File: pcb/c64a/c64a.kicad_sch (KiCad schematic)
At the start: 146 parts, among them J1 Conn_01x20_Male, SW1 1, SW10 3, SW11 W, SW12 A, SW13 L-SHIFT, SW14 Z, SW15 S, SW16 E, SW17 4, SW18 5, SW19 R, SW2 L-ARROW, SW20 D, SW21 X, SW22 C, SW23 F, SW24 T, SW25 6, SW26 7, SW27 Y, SW28 G, SW29 V, SW3 CTRL, SW30 B, SW31 H, SW32 U, SW33 8, SW34 9, SW35 I, SW36 J, SW37 N, SW38 M, SW39 K, SW4 RUN / STOP, SW40 O, SW41 0, SW42 +, SW43 P, SW44 L, SW45 ,, SW46 ., SW47 :, SW48 @, SW49 -, SW5 SPACE, SW50 POUND, SW51 *, SW52 ;, SW53 /, SW54 R-SHIFT, SW55 =, SW56 UP-ARROW, SW57 HOME, SW58 RESTORE, SW59 DEL, SW6 COMMODORE, SW60 RETURN, SW61 LEFT-RIGHT, SW62 UP-DOWN, SW63 F1, SW64 F3, SW65 F5, SW66 F7, SW7 Q, SW8 2, SW9 SHIFT-LOCK

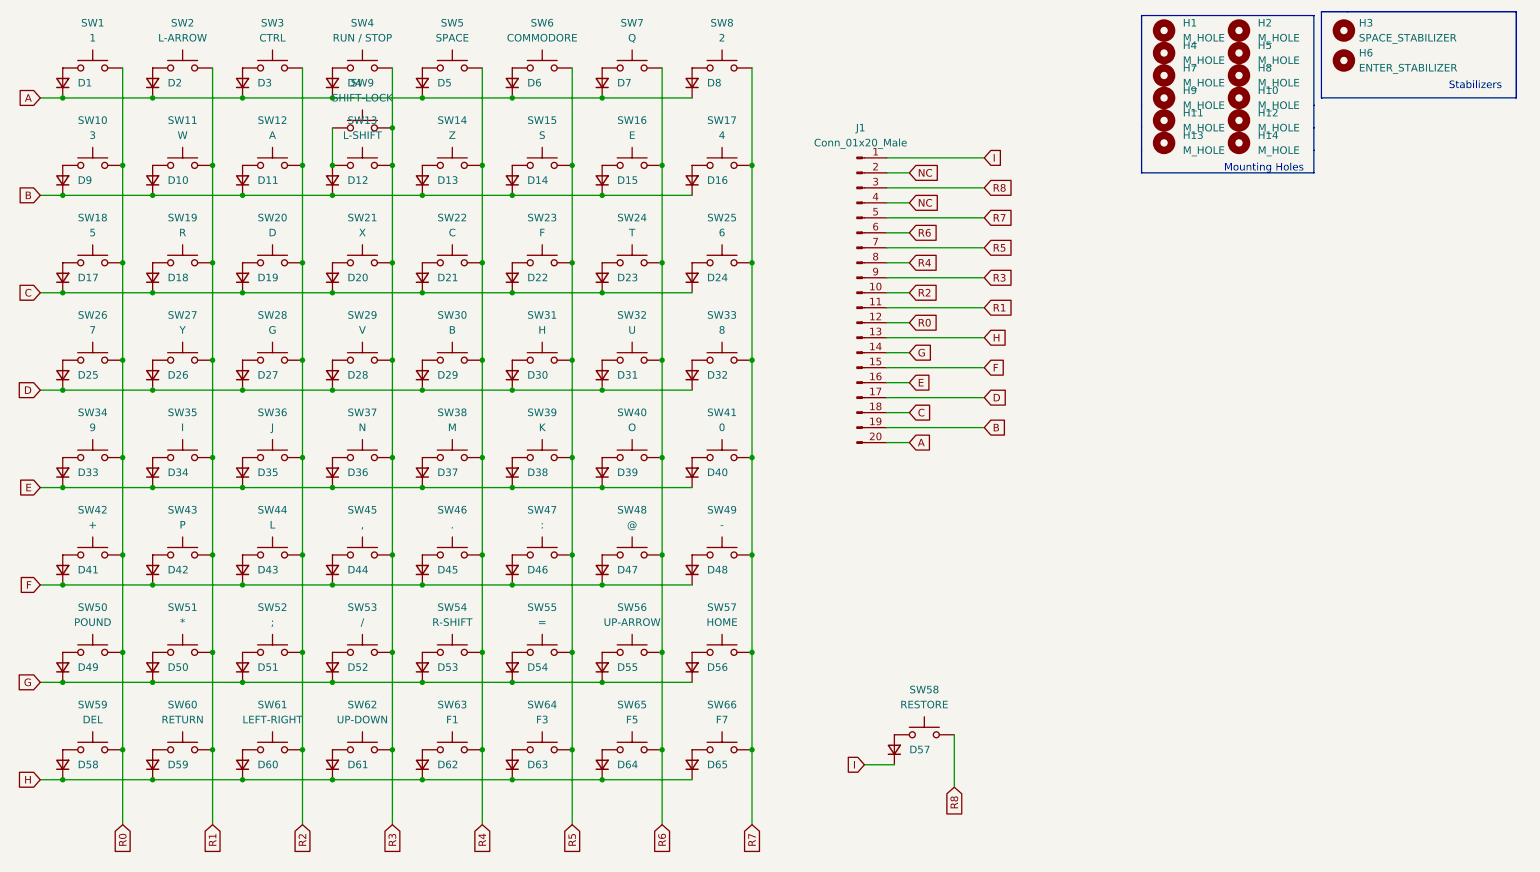
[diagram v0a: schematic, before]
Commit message: Switches changed to 5 pin
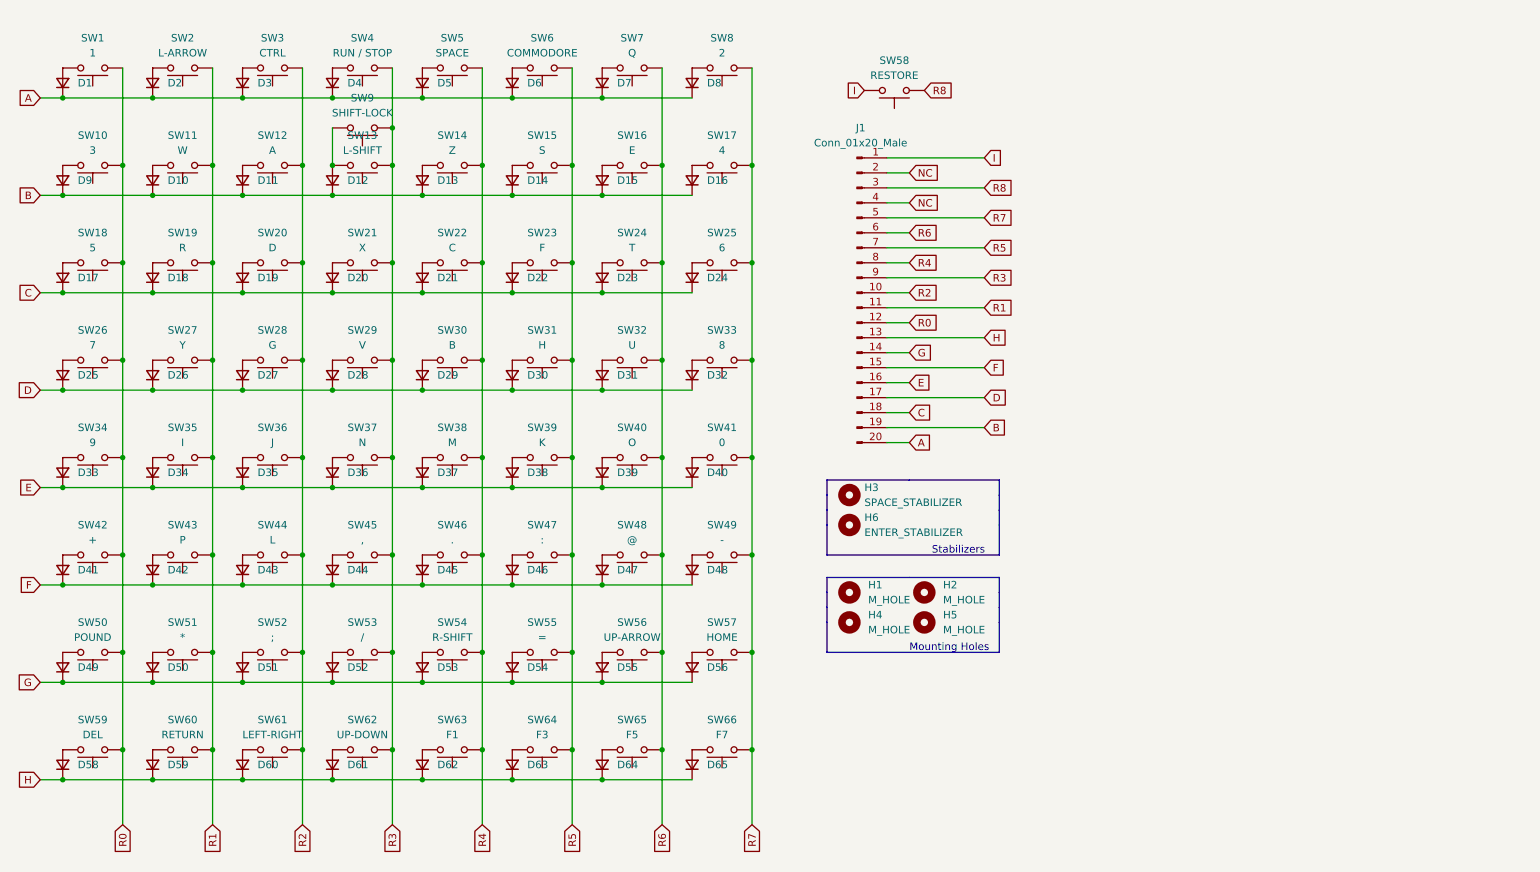
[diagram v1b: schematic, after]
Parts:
- removed D57: D_Small, Diode_SMD:D_SOD-123, symbol Device:D_Small
- removed H10, H11, H12, H13, H14, H7, H8, H9: M_HOLE, MountingHole:MountingHole_2.2mm_M2, symbol Mechanical:MountingHole
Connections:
- net I: now also SW58.2
- net R0: now also SW1.1, SW10.1, SW18.1, SW26.1, SW34.1, SW42.1, SW50.1, SW59.1; no longer SW1.2, SW10.2, SW18.2, SW26.2, SW34.2, SW42.2, SW50.2, SW59.2
- net R1: now also SW11.1, SW19.1, SW2.1, SW27.1, SW35.1, SW43.1, SW51.1, SW60.1; no longer SW11.2, SW19.2, SW2.2, SW27.2, SW35.2, SW43.2, SW51.2, SW60.2
- net R2: now also SW12.1, SW20.1, SW28.1, SW3.1, SW36.1, SW44.1, SW52.1, SW61.1; no longer SW12.2, SW20.2, SW28.2, SW3.2, SW36.2, SW44.2, SW52.2, SW61.2
- net R3: now also SW13.1, SW21.1, SW29.1, SW37.1, SW4.1, SW45.1, SW53.1, SW62.1, SW9.1; no longer SW13.2, SW21.2, SW29.2, SW37.2, SW4.2, SW45.2, SW53.2, SW62.2, SW9.2
- net R4: now also SW14.1, SW22.1, SW30.1, SW38.1, SW46.1, SW5.1, SW54.1, SW63.1; no longer SW14.2, SW22.2, SW30.2, SW38.2, SW46.2, SW5.2, SW54.2, SW63.2
- net R5: now also SW15.1, SW23.1, SW31.1, SW39.1, SW47.1, SW55.1, SW6.1, SW64.1; no longer SW15.2, SW23.2, SW31.2, SW39.2, SW47.2, SW55.2, SW6.2, SW64.2
- net R6: now also SW16.1, SW24.1, SW32.1, SW40.1, SW48.1, SW56.1, SW65.1, SW7.1; no longer SW16.2, SW24.2, SW32.2, SW40.2, SW48.2, SW56.2, SW65.2, SW7.2
- net R7: now also SW17.1, SW25.1, SW33.1, SW41.1, SW49.1, SW57.1, SW66.1, SW8.1; no longer SW17.2, SW25.2, SW33.2, SW41.2, SW49.2, SW57.2, SW66.2, SW8.2
- net R8: now also SW58.1; no longer SW58.2
- net at D11.2 (A): now also SW12.2; no longer SW12.1
- net at D63.2 (A): now also SW64.2; no longer SW64.1
- net at D22.2 (A): now also SW23.2; no longer SW23.1
- net at D48.2 (A): now also SW49.2; no longer SW49.1
- net at D15.2 (A): now also SW16.2; no longer SW16.1
- net at D9.2 (A): now also SW10.2; no longer SW10.1
- net at D4.2 (A): now also SW4.2; no longer SW4.1
- net at D6.2 (A): now also SW6.2; no longer SW6.1
- net at D37.2 (A): now also SW38.2; no longer SW38.1
- net at D54.2 (A): now also SW55.2; no longer SW55.1
- net at D39.2 (A): now also SW40.2; no longer SW40.1
- net at D35.2 (A): now also SW36.2; no longer SW36.1
- net at D26.2 (A): now also SW27.2; no longer SW27.1
- net at D47.2 (A): now also SW48.2; no longer SW48.1
- net at D8.2 (A): now also SW8.2; no longer SW8.1
- net at D59.2 (A): now also SW60.2; no longer SW60.1
- net at D41.2 (A): now also SW42.2; no longer SW42.1
- net at D17.2 (A): now also SW18.2; no longer SW18.1
- net at D10.2 (A): now also SW11.2; no longer SW11.1
- net at D53.2 (A): now also SW54.2; no longer SW54.1
- net at D20.2 (A): now also SW21.2; no longer SW21.1
- net at D40.2 (A): now also SW41.2; no longer SW41.1
- net at D34.2 (A): now also SW35.2; no longer SW35.1
- net at D65.2 (A): now also SW66.2; no longer SW66.1
- net at D55.2 (A): now also SW56.2; no longer SW56.1
- net at D27.2 (A): now also SW28.2; no longer SW28.1
- net at D46.2 (A): now also SW47.2; no longer SW47.1
- net at D58.2 (A): now also SW59.2; no longer SW59.1
- net at D38.2 (A): now also SW39.2; no longer SW39.1
- net at D62.2 (A): now also SW63.2; no longer SW63.1
- net at D3.2 (A): now also SW3.2; no longer SW3.1
- net at D30.2 (A): now also SW31.2; no longer SW31.1
- net at D44.2 (A): now also SW45.2; no longer SW45.1
- net at D25.2 (A): now also SW26.2; no longer SW26.1
- net at D43.2 (A): now also SW44.2; no longer SW44.1
- net at D19.2 (A): now also SW20.2; no longer SW20.1
- net at D29.2 (A): now also SW30.2; no longer SW30.1
- net at D31.2 (A): now also SW32.2; no longer SW32.1
- net at D28.2 (A): now also SW29.2; no longer SW29.1
- net at D51.2 (A): now also SW52.2; no longer SW52.1
- net at D21.2 (A): now also SW22.2; no longer SW22.1
- net at D45.2 (A): now also SW46.2; no longer SW46.1
- net at D1.2 (A): now also SW1.2; no longer SW1.1
- net at D5.2 (A): now also SW5.2; no longer SW5.1
- net at D52.2 (A): now also SW53.2; no longer SW53.1
- net at D36.2 (A): now also SW37.2; no longer SW37.1
- net at D7.2 (A): now also SW7.2; no longer SW7.1
- net at D2.2 (A): now also SW2.2; no longer SW2.1
- net at D64.2 (A): now also SW65.2; no longer SW65.1
- net at D16.2 (A): now also SW17.2; no longer SW17.1
- net at D60.2 (A): now also SW61.2; no longer SW61.1
- net at D56.2 (A): now also SW57.2; no longer SW57.1
- net at D61.2 (A): now also SW62.2; no longer SW62.1
- net at D24.2 (A): now also SW25.2; no longer SW25.1
- net at D13.2 (A): now also SW14.2; no longer SW14.1
- net at D49.2 (A): now also SW50.2; no longer SW50.1
- net at D14.2 (A): now also SW15.2; no longer SW15.1
- net at D18.2 (A): now also SW19.2; no longer SW19.1
- net at D23.2 (A): now also SW24.2; no longer SW24.1
- net at D33.2 (A): now also SW34.2; no longer SW34.1
- net at D42.2 (A): now also SW43.2; no longer SW43.1
- net at D32.2 (A): now also SW33.2; no longer SW33.1
- net at D50.2 (A): now also SW51.2; no longer SW51.1
- new net: D12.2 (A), SW13.2, SW9.2
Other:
- moved on the sheet: H1, H2, H3, H4, H5, H6, SW1, SW10, SW11, SW12, SW13, SW14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

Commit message: Mount cover + pcb fixes
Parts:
- J1: footprint Connector_PinHeader_1.00mm:PinHeader_1x20_P1.00mm_Horizontal -> Connector_PinHeader_1.27mm:PinHeader_1x20_P1.27mm_Horizontal
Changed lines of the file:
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@@
     (property "Reference" "J1" (id 0) (at 170.815 35.56 0))
     (property "Value" "Conn_01x20_Male" (id 1) (at 170.815 38.1 0))
-    (property "Footprint" "Connector_PinHeader_1.00mm:PinHeader_1x20_P1.00mm_Horizontal" (id 2) (at 170.18 63.5 0)
+    (property "Footprint" "Connector_PinHeader_1.27mm:PinHeader_1x20_P1.27mm_Horizontal" (id 2) (at 170.18 63.5 0)
       (effects (font (size 1.27 1.27)) hide)
     )
@@
     )
     (path "/50d77f76-2263-4e5b-952f-03c8b908276f"
-      (reference "J1") (unit 1) (value "Conn_01x20_Male") (footprint "Connector_PinHeader_1.00mm:PinHeader_1x20_P1.00mm_Horizontal")
+      (reference "J1") (unit 1) (value "Conn_01x20_Male") (footprint "Connector_PinHeader_1.27mm:PinHeader_1x20_P1.27mm_Horizontal")
     )
     (path "/6b258f22-926d-4192-b794-d0d003b1d1f3"

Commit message: Fixing spacing issues
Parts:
- removed H1, H2, H4, H5: M_HOLE, MountingHole:MountingHole_2.2mm_M2, symbol Mechanical:MountingHole
- J1: footprint Connector_PinHeader_1.27mm:PinHeader_1x20_P1.27mm_Horizontal -> Connector_PinHeader_2.54mm:PinHeader_1x20_P2.54mm_Horizontal
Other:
- note removed: "Mounting Holes"
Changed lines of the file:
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@@
   (junction (at 45.72 58.42) (diameter 0) (color 0 0 0 0)
   )
-  (polyline (pts (xy 194.31 124.46) (xy 165.1 124.46))
-    (stroke (width 0) (type default) (color 0 0 0 0))
-  )
   (wire (pts (xy 31.75 63.5) (xy 35.56 63.5))
     (stroke (width 0) (type default) (color 0 0 0 0))
@@
     (stroke (width 0) (type default) (color 0 0 0 0))
   )
-  (polyline (pts (xy 165.1 111.76) (xy 179.07 111.76))
-    (stroke (width 0) (type default) (color 0 0 0 0))
-  )
   (wire (pts (xy 96.52 46.99) (xy 111.76 46.99))
     (stroke (width 0) (type default) (color 0 0 0 0))
@@
     (stroke (width 0) (type default) (color 0 0 0 0))
   )
-  (polyline (pts (xy 165.1 124.46) (xy 165.1 119.38))
-    (stroke (width 0) (type default) (color 0 0 0 0))
-  )
   (wire (pts (xy 96.52 129.54) (xy 111.76 129.54))
     (stroke (width 0) (type default) (color 0 0 0 0))
@@
     (stroke (width 0) (type default) (color 0 0 0 0))
   )
-  (polyline (pts (xy 194.31 111.76) (xy 194.31 114.3))
-    (stroke (width 0) (type default) (color 0 0 0 0))
-  )
   (wire (pts (xy 111.76 96.52) (xy 127 96.52))
     (stroke (width 0) (type default) (color 0 0 0 0))
@@
     (stroke (width 0) (type default) (color 0 0 0 0))
   )
-  (polyline (pts (xy 194.31 114.3) (xy 194.31 116.84))
-    (stroke (width 0) (type default) (color 0 0 0 0))
-  )
   (wire (pts (xy 152.4 74.93) (xy 152.4 91.44))
     (stroke (width 0) (type default) (color 0 0 0 0))
   )
-  (polyline (pts (xy 165.1 119.38) (xy 165.1 116.84))
-    (stroke (width 0) (type default) (color 0 0 0 0))
-  )
   (wire (pts (xy 31.75 96.52) (xy 35.56 96.52))
     (stroke (width 0) (type default) (color 0 0 0 0))
@@
     (stroke (width 0) (type default) (color 0 0 0 0))
   )
-  (polyline (pts (xy 165.1 116.84) (xy 165.1 114.3))
-    (stroke (width 0) (type default) (color 0 0 0 0))
-  )
   (wire (pts (xy 179.07 63.5) (xy 175.26 63.5))
     (stroke (width 0) (type default) (color 0 0 0 0))
@@
     (stroke (width 0) (type default) (color 0 0 0 0))
   )
-  (polyline (pts (xy 165.1 114.3) (xy 165.1 111.76))
-    (stroke (width 0) (type default) (color 0 0 0 0))
-  )
   (polyline (pts (xy 179.07 95.25) (xy 194.31 95.25))
     (stroke (width 0) (type default) (color 0 0 0 0))
@@
     (stroke (width 0) (type default) (color 0 0 0 0))
   )
-  (polyline (pts (xy 194.31 116.84) (xy 194.31 119.38))
-    (stroke (width 0) (type default) (color 0 0 0 0))
-  )
   (wire (pts (xy 45.72 58.42) (xy 45.72 74.93))
     (stroke (width 0) (type default) (color 0 0 0 0))
@@
     (stroke (width 0) (type default) (color 0 0 0 0))
   )
-  (polyline (pts (xy 179.07 111.76) (xy 194.31 111.76))
-    (stroke (width 0) (type default) (color 0 0 0 0))
-  )
   (wire (pts (xy 81.28 146.05) (xy 96.52 146.05))
     (stroke (width 0) (type default) (color 0 0 0 0))
@@
     (stroke (width 0) (type default) (color 0 0 0 0))
   )
-  (polyline (pts (xy 194.31 119.38) (xy 194.31 124.46))
-    (stroke (width 0) (type default) (color 0 0 0 0))
-  )
   (wire (pts (xy 76.2 74.93) (xy 76.2 91.44))
     (stroke (width 0) (type default) (color 0 0 0 0))
@@
   (wire (pts (xy 179.07 73.66) (xy 175.26 73.66))
     (stroke (width 0) (type default) (color 0 0 0 0))
-  )
-  (text "Mounting Holes" (at 179.07 124.46 0)
-    (effects (font (size 1.27 1.27)) (justify left bottom))
   )
   (text "Stabilizers" (at 182.88 107.95 0)
@@
     (property "Reference" "J1" (id 0) (at 170.815 35.56 0))
     (property "Value" "Conn_01x20_Male" (id 1) (at 170.815 38.1 0))
-    (property "Footprint" "Connector_PinHeader_1.27mm:PinHeader_1x20_P1.27mm_Horizontal" (id 2) (at 170.18 63.5 0)
+    (property "Footprint" "Connector_PinHeader_2.54mm:PinHeader_1x20_P2.54mm_Horizontal" (id 2) (at 170.18 63.5 0)
       (effects (font (size 1.27 1.27)) hide)
     )
@@
     (pin "2")
   )
-  (symbol (lib_id "Mechanical:MountingHole") (at 168.91 114.3 0) (unit 1)
-    (in_bom yes) (on_board yes) (fields_autoplaced)
-    (property "Reference" "H1" (id 0) (at 172.085 113.0299 0)
-      (effects (font (size 1.27 1.27)) (justify left))
-    )
-    (property "Value" "M_HOLE" (id 1) (at 172.085 115.5699 0)
-      (effects (font (size 1.27 1.27)) (justify left))
-    )
-    (property "Footprint" "MountingHole:MountingHole_2.2mm_M2" (id 2) (at 168.91 114.3 0)
-      (effects (font (size 1.27 1.27)) hide)
-    )
-    (property "Datasheet" "~" (id 3) (at 168.91 114.3 0)
-      (effects (font (size 1.27 1.27)) hide)
-    )
-  )
   (symbol (lib_id "Device:D_Small") (at 81.28 44.45 90) (unit 1)
     (in_bom yes) (on_board yes)
@@
     (pin "2")
   )
-  (symbol (lib_id "Mechanical:MountingHole") (at 168.91 119.38 0) (unit 1)
-    (in_bom yes) (on_board yes)
-    (property "Reference" "H4" (id 0) (at 172.085 118.1099 0)
-      (effects (font (size 1.27 1.27)) (justify left))
-    )
-    (property "Value" "M_HOLE" (id 1) (at 172.085 120.6499 0)
-      (effects (font (size 1.27 1.27)) (justify left))
-    )
-    (property "Footprint" "MountingHole:MountingHole_2.2mm_M2" (id 2) (at 168.91 119.38 0)
-      (effects (font (size 1.27 1.27)) hide)
-    )
-    (property "Datasheet" "~" (id 3) (at 168.91 119.38 0)
-      (effects (font (size 1.27 1.27)) hide)
-    )
-  )
   (symbol (lib_id "Device:D_Small") (at 81.28 127 90) (unit 1)
     (in_bom yes) (on_board yes)
@@
     (pin "2")
   )
-  (symbol (lib_id "Mechanical:MountingHole") (at 181.61 119.38 0) (unit 1)
-    (in_bom yes) (on_board yes)
-    (property "Reference" "H5" (id 0) (at 184.785 118.1099 0)
-      (effects (font (size 1.27 1.27)) (justify left))
-    )
-    (property "Value" "M_HOLE" (id 1) (at 184.785 120.6499 0)
-      (effects (font (size 1.27 1.27)) (justify left))
-    )
-    (property "Footprint" "MountingHole:MountingHole_2.2mm_M2" (id 2) (at 181.61 119.38 0)
-      (effects (font (size 1.27 1.27)) hide)
-    )
-    (property "Datasheet" "~" (id 3) (at 181.61 119.38 0)
-      (effects (font (size 1.27 1.27)) hide)
-    )
-  )
   (symbol (lib_id "Device:D_Small") (at 66.04 77.47 90) (unit 1)
     (in_bom yes) (on_board yes)
@@
     (pin "2")
   )
-  (symbol (lib_id "Mechanical:MountingHole") (at 181.61 114.3 0) (unit 1)
-    (in_bom yes) (on_board yes) (fields_autoplaced)
-    (property "Reference" "H2" (id 0) (at 184.785 113.0299 0)
-      (effects (font (size 1.27 1.27)) (justify left))
-    )
-    (property "Value" "M_HOLE" (id 1) (at 184.785 115.5699 0)
-      (effects (font (size 1.27 1.27)) (justify left))
-    )
-    (property "Footprint" "MountingHole:MountingHole_2.2mm_M2" (id 2) (at 181.61 114.3 0)
-      (effects (font (size 1.27 1.27)) hide)
-    )
-    (property "Datasheet" "~" (id 3) (at 181.61 114.3 0)
-      (effects (font (size 1.27 1.27)) hide)
-    )
-  )
   (symbol (lib_id "Switch:SW_Push") (at 86.36 91.44 180) (unit 1)
     (in_bom yes) (on_board yes) (fields_autoplaced)
@@
       (reference "D65") (unit 1) (value "D_Small") (footprint "Diode_SMD:D_SOD-123")
     )
-    (path "/5c0b23f2-203a-4182-94e3-5277128c45dc"
-      (reference "H1") (unit 1) (value "M_HOLE") (footprint "MountingHole:MountingHole_2.2mm_M2")
-    )
-    (path "/c5b50c1f-cc5b-4914-aa15-df909ae3eb94"
-      (reference "H2") (unit 1) (value "M_HOLE") (footprint "MountingHole:MountingHole_2.2mm_M2")
-    )
     (path "/145c11b9-1bdc-4693-9d2e-9955fd7b97f7"
       (reference "H3") (unit 1) (value "SPACE_STABILIZER") (footprint "Mounting_Keyboard_Stabilizer:Stabilizer_Cherry_MX_9.00u")
     )
-    (path "/70035f6c-c2c4-4801-ac68-1bcfc3cbad1a"
-      (reference "H4") (unit 1) (value "M_HOLE") (footprint "MountingHole:MountingHole_2.2mm_M2")
-    )
-    (path "/86c53dca-b13d-4b0f-9719-70b12b954d3c"
-      (reference "H5") (unit 1) (value "M_HOLE") (footprint "MountingHole:MountingHole_2.2mm_M2")
-    )
     (path "/90203188-a65e-466d-a2ed-515dc2020f60"
       (reference "H6") (unit 1) (value "ENTER_STABILIZER") (footprint "bschwind_stabilizers:cherry_mx_stabilizer_2.00u")
     )
     (path "/50d77f76-2263-4e5b-952f-03c8b908276f"
-      (reference "J1") (unit 1) (value "Conn_01x20_Male") (footprint "Connector_PinHeader_1.27mm:PinHeader_1x20_P1.27mm_Horizontal")
+      (reference "J1") (unit 1) (value "Conn_01x20_Male") (footprint "Connector_PinHeader_2.54mm:PinHeader_1x20_P2.54mm_Horizontal")
     )
     (path "/6b258f22-926d-4192-b794-d0d003b1d1f3"
